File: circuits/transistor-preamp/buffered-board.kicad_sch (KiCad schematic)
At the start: 21 parts, among them J1 Conn_01x02, J2 Conn_01x02, J3 Conn_01x02, Q1 2N3904, Q2 2N3904

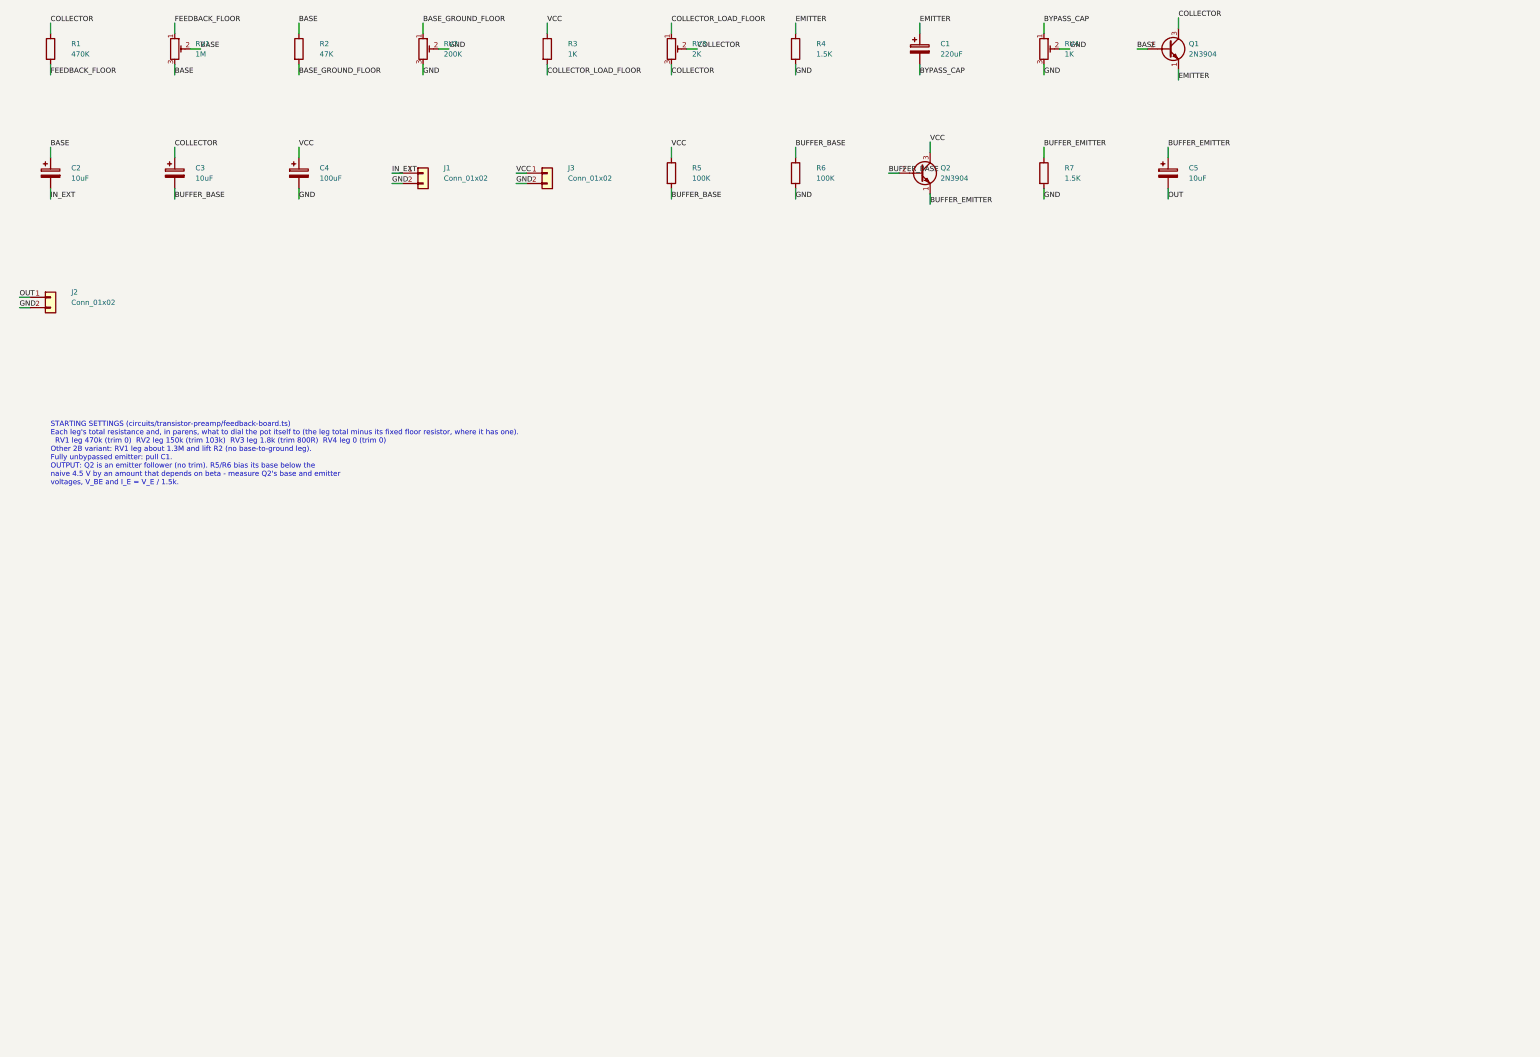
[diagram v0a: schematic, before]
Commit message: schematic layout
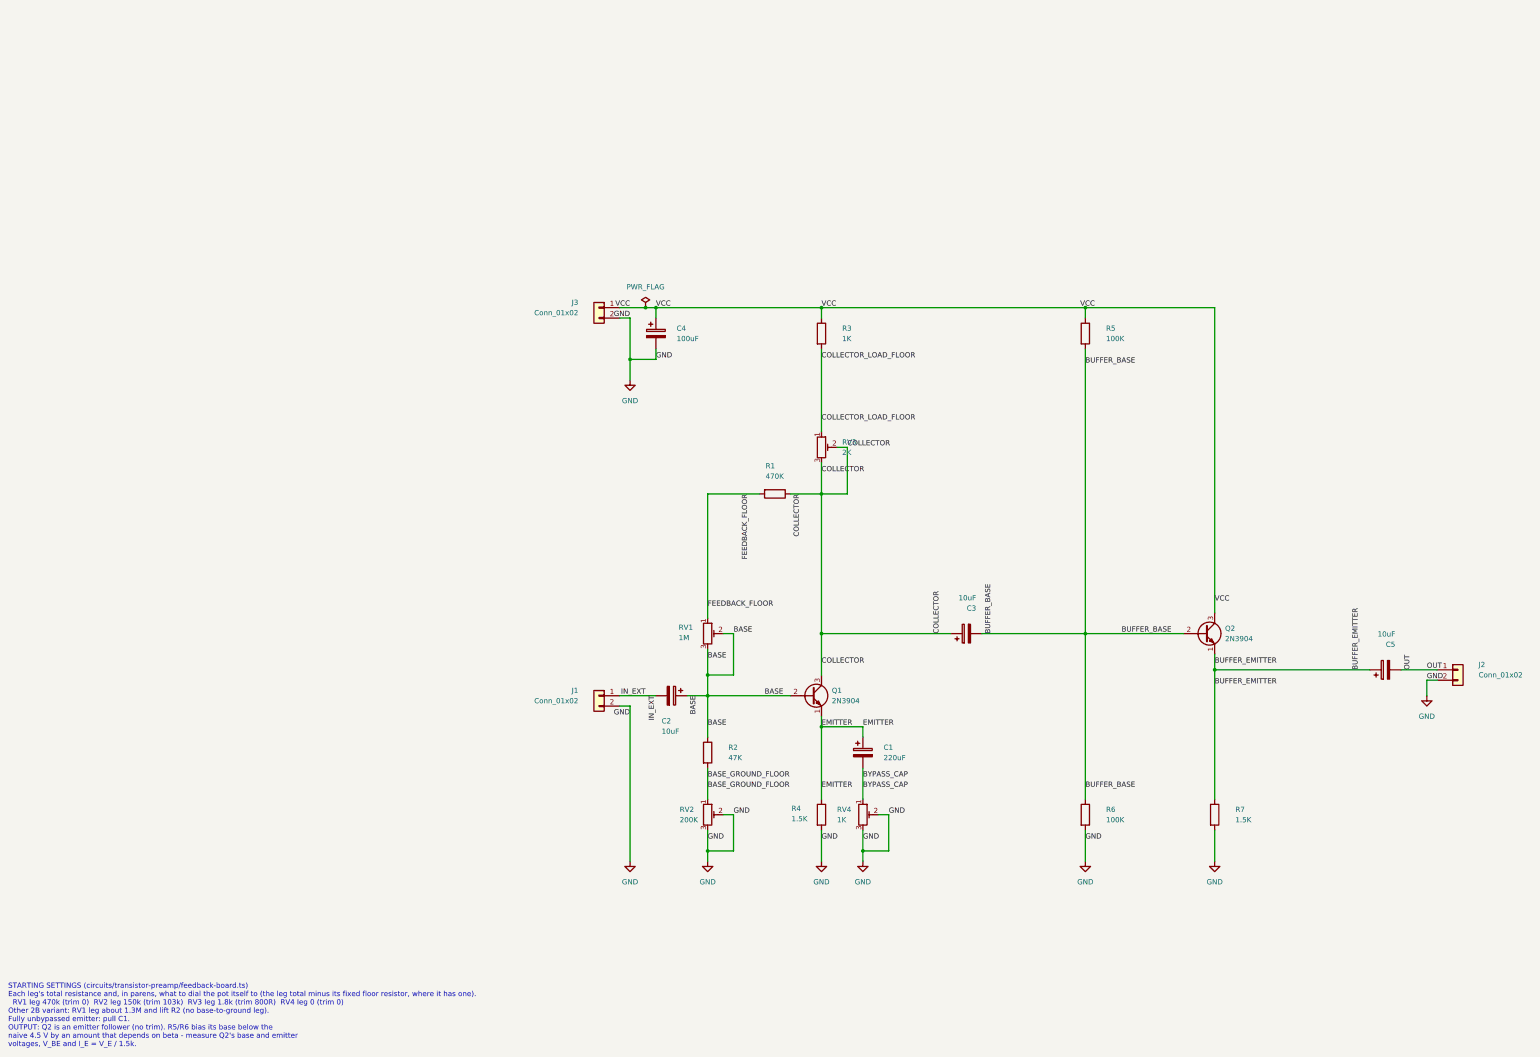
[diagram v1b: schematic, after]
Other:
- moved on the sheet: C1, C2, C3, C4, C5, J1, J2, J3, Q1, Q2, R1, R2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
